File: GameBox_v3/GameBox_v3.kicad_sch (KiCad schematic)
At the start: 22 parts, among them J1 OLED, J2 Conn_01x08, SW1 ON/OFF, SW2 SW_up, SW3 SW_down, SW4 SW_right, SW5 SW_left, SW6 SW_select, U1 ATmega328P-A, U2 3.3V_boost_regulator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

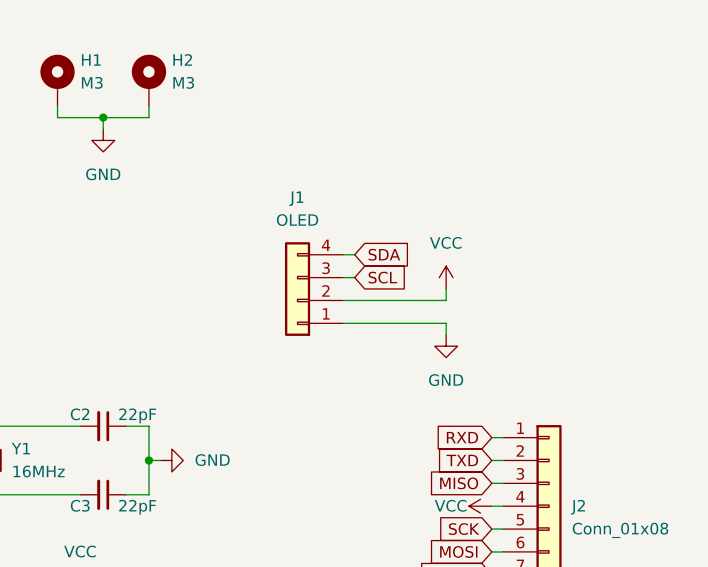
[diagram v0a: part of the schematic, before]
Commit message: fixed OLEDs
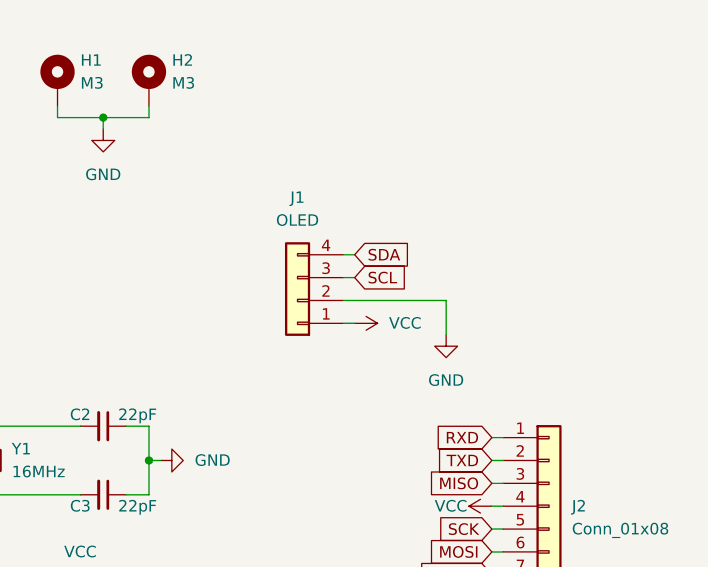
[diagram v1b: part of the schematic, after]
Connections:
- net GND: now also J1.2 (Pin_2); no longer J1.1 (Pin_1)
- net VCC: now also J1.1 (Pin_1); no longer J1.2 (Pin_2)
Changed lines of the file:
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@@
-    (stroke (width 0) (type default) (color 0 0 0 0))
-  )
-  (wire (pts (xy 198.12 87.63) (xy 209.55 87.63))
     (stroke (width 0) (type default) (color 0 0 0 0))
   )
@@
     (stroke (width 0) (type default) (color 0 0 0 0))
   )
-  (wire (pts (xy 209.55 87.63) (xy 209.55 88.9))
+  (wire (pts (xy 209.55 85.09) (xy 209.55 88.9))
     (stroke (width 0) (type default) (color 0 0 0 0))
   )
@@
     (stroke (width 0) (type default) (color 0 0 0 0))
   )
-  (wire (pts (xy 198.12 85.09) (xy 209.55 85.09))
+  (wire (pts (xy 198.12 87.63) (xy 199.39 87.63))
     (stroke (width 0) (type default) (color 0 0 0 0))
   )
@@
     (stroke (width 0) (type default) (color 0 0 0 0))
   )
-  (wire (pts (xy 209.55 85.09) (xy 209.55 83.82))
-    (stroke (width 0) (type default) (color 0 0 0 0))
-  )
   (wire (pts (xy 152.4 106.68) (xy 157.48 106.68))
     (stroke (width 0) (type default) (color 0 0 0 0))
@@
     (stroke (width 0) (type default) (color 0 0 0 0))
   )
+  (wire (pts (xy 209.55 85.09) (xy 198.12 85.09))
+    (stroke (width 0) (type default) (color 0 0 0 0))
+  )
   (wire (pts (xy 168.91 119.38) (xy 167.64 119.38))
     (stroke (width 0) (type default) (color 0 0 0 0))
@@
     )
   )
-  (symbol (lib_id "power:VCC") (at 209.55 83.82 0) (unit 1)
+  (symbol (lib_id "power:VCC") (at 199.39 87.63 270) (unit 1)
     (in_bom yes) (on_board yes) (fields_autoplaced)
-    (property "Reference" "#PWR06" (id 0) (at 209.55 87.63 0)
+    (property "Reference" "#PWR06" (id 0) (at 195.58 87.63 0)
       (effects (font (size 1.27 1.27)) hide)
     )
-    (property "Value" "VCC" (id 1) (at 209.55 78.74 0))
-    (property "Footprint" "" (id 2) (at 209.55 83.82 0)
+    (property "Value" "VCC" (id 1) (at 203.2 87.6299 90)
+      (effects (font (size 1.27 1.27)) (justify left))
+    )
+    (property "Footprint" "" (id 2) (at 199.39 87.63 0)
       (effects (font (size 1.27 1.27)) hide)
     )
-    (property "Datasheet" "" (id 3) (at 209.55 83.82 0)
+    (property "Datasheet" "" (id 3) (at 199.39 87.63 0)
       (effects (font (size 1.27 1.27)) hide)
     )
